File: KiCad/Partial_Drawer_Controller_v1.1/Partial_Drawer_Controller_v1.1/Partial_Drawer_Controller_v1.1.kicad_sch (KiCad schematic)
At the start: 69 parts, among them J1 Conn_02x03_Odd_Even, J2 Conn_02x04_Odd_Even, J3 Conn_02x05_Odd_Even, U1 PESD2CANFD24L-TR, X1 Conn_01x04_2.5mm_JST_S04B-XAS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, X10 Conn_01x03_3.0mm_Molex_Micro_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, X11 Conn_01x03_3.0mm_Molex_Micro_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, X12 Conn_01x04_2.5mm_JST_S04B-XAS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, X13 Conn_01x03_2.5mm_JST_S04B-XAS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, X2 Conn_01x02_2.5mm_JST_S02B-XAS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

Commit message: fix: adds important hint about usage of IO2 for flashing the ESP32
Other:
- note added: "TODO: IO2 needs to be pulled low during flash, this is not the case when using Drawer_1_Encoder_B here!!"
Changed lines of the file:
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@@
+		)
+	)
+	(text "TODO: IO2 needs to be pulled low during flash,\nthis is not the case when using Drawer_1_Encoder_B\nhere!!"
+		(exclude_from_sim no)
+		(at 219.71 18.796 0)
+		(effects
+			(font
+				(size 1.27 1.27)
+				(thickness 0.254)
+				(bold yes)
+				(color 255 0 0 1)
+			)
 		)
 	)

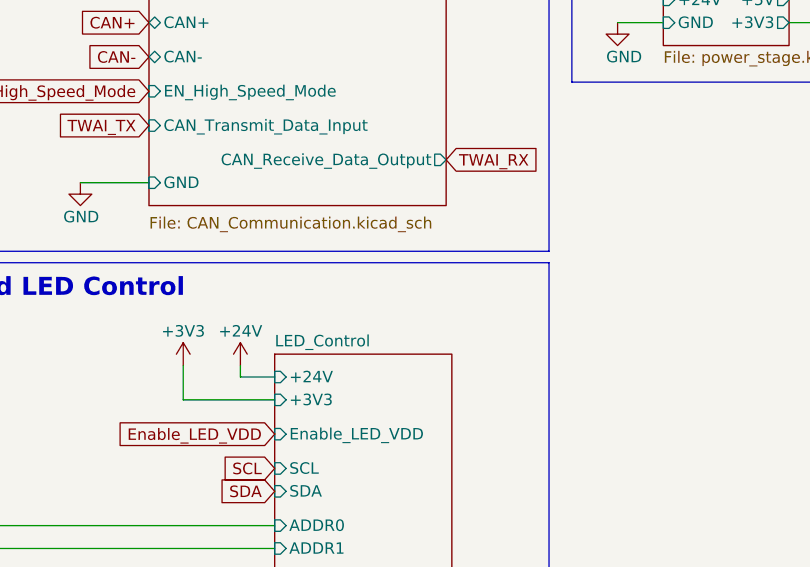
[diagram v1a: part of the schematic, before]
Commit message: docs: moves TODO to `Partial_Drawer_Controller_v1.1`
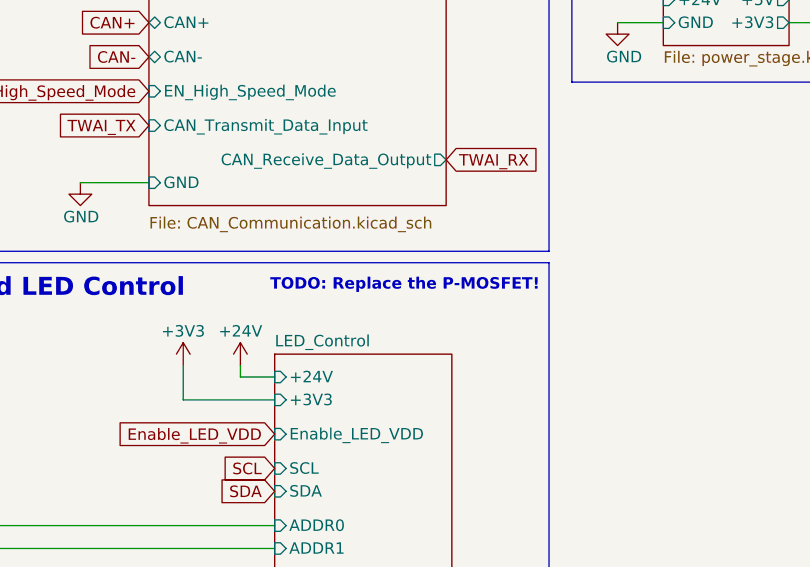
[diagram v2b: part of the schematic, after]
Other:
- note added: "TODO: Replace the P-MOSFET!"

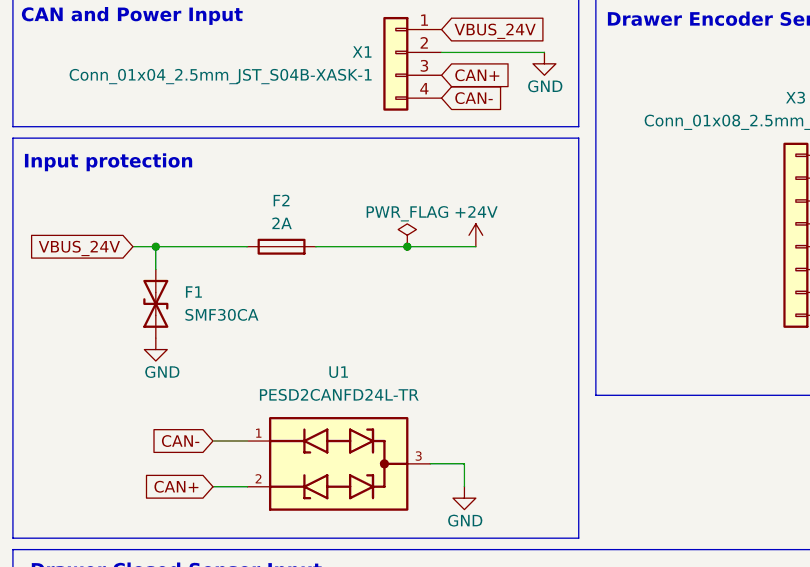
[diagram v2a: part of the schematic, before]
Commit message: docs: adds TODO for reverse voltage protection
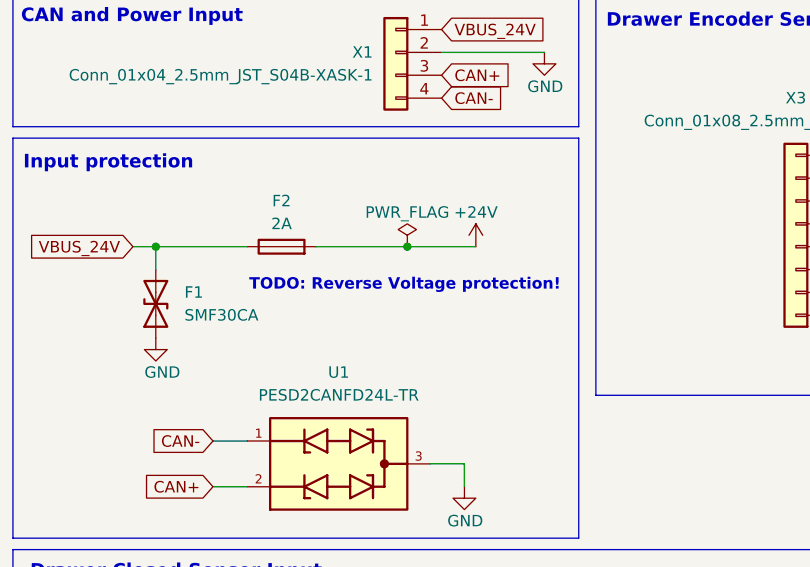
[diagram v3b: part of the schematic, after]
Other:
- note added: "TODO: Reverse Voltage protection!"
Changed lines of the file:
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@@
+		)
+	)
+	(text "TODO: Reverse Voltage protection!"
+		(exclude_from_sim no)
+		(at 59.436 53.848 0)
+		(effects
+			(font
+				(size 1.27 1.27)
+				(thickness 0.254)
+				(bold yes)
+				(color 255 0 0 1)
+			)
 		)
 	)
